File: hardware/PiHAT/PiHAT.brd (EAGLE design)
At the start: 65 x 56.5 mm, 41 parts, among them U1 ATMEGA328P, U2 TSL2561, U3 OPA344, U4 MPL115A, U6 ADMP401, U7 SHT31-DIS, Y1 16MHZ

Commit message: Update
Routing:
- net GND: vias 3 -> 4
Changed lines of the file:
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@@
 <via x="27.3812" y="10.795" extent="1-16" drill="0.6"/>
 <via x="39.243" y="6.3246" extent="1-16" drill="0.6"/>
-<wire x1="26.6256" y1="21.0058" x2="28.2256" y2="21.0058" width="0" layer="19" extent="1-1"/>
+<via x="26.162" y="30.5308" extent="1-16" drill="0.6"/>
 </signal>
 <signal name="GPIO18">

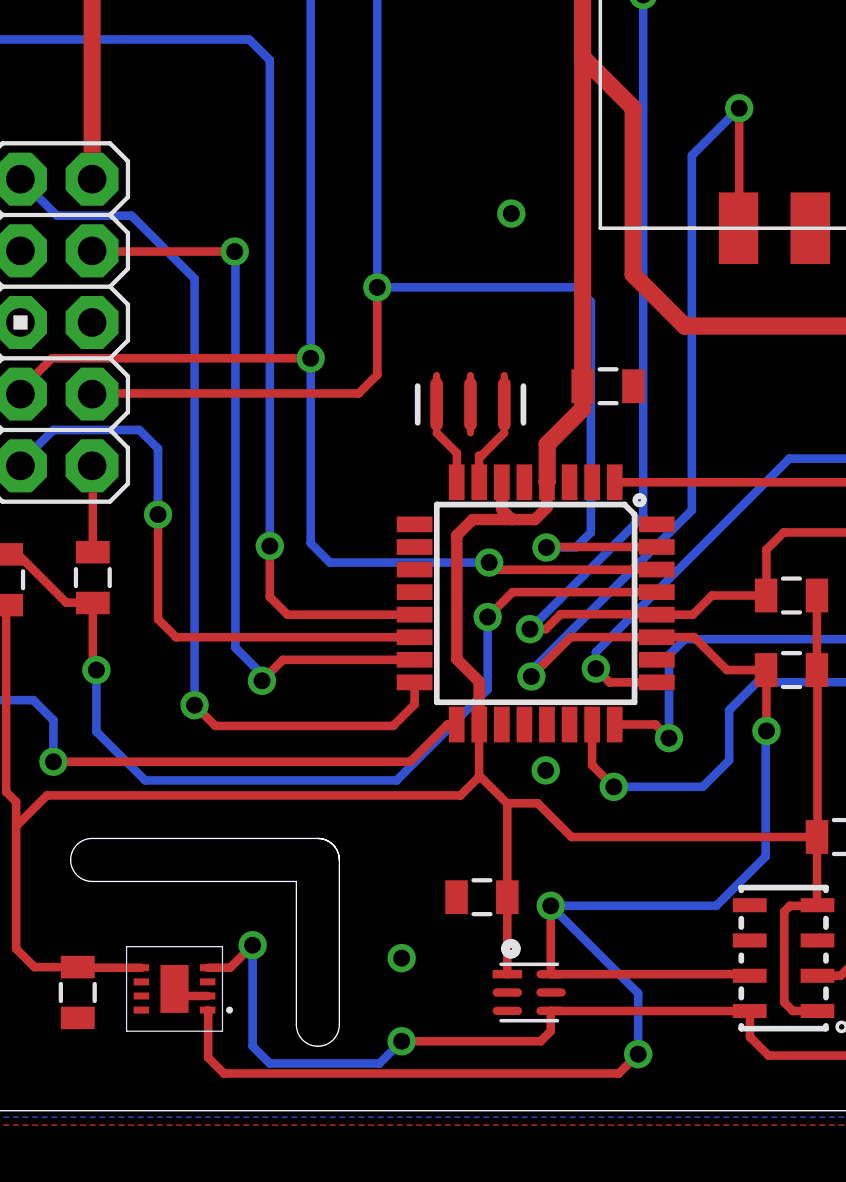
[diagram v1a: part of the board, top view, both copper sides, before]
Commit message: Moved Trace on PiAQ, v4 of enclosure
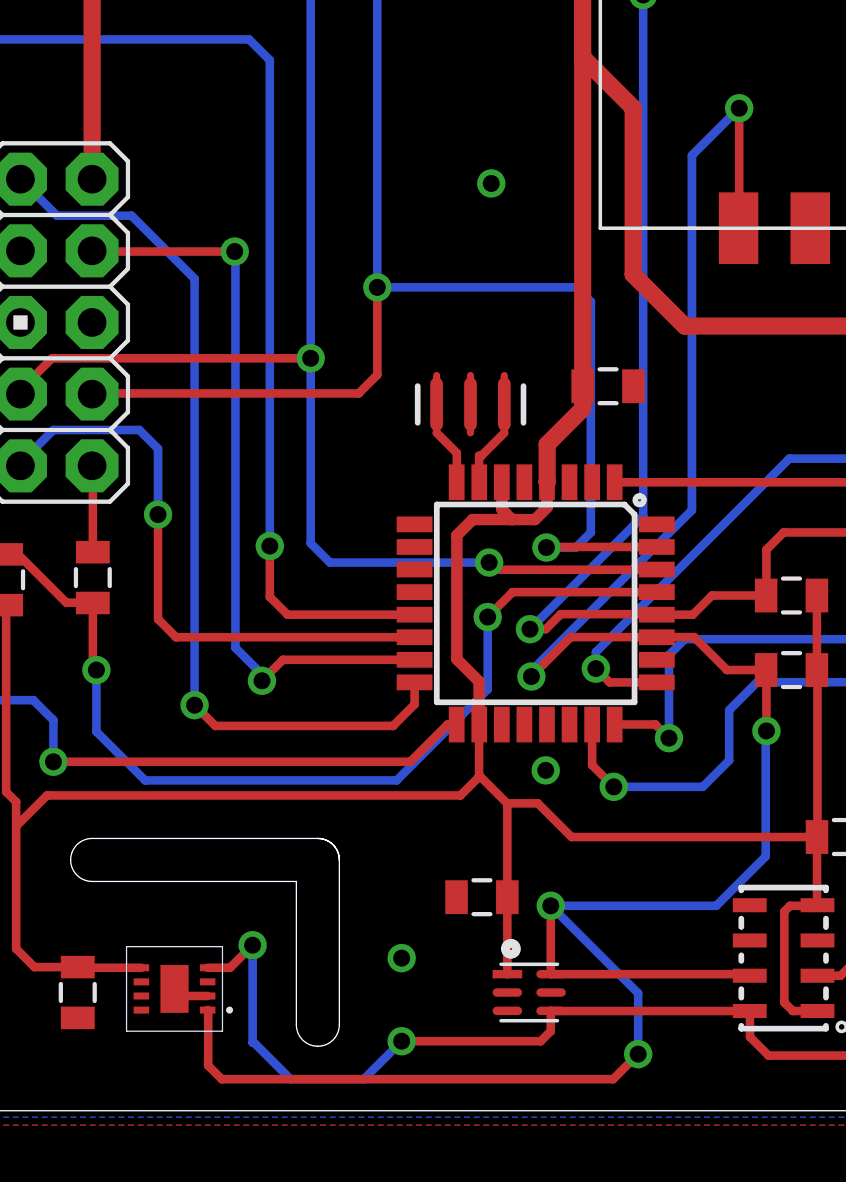
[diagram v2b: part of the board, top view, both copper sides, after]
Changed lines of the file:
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@@
 <layer number="23" name="tOrigins" color="14" fill="1" visible="yes" active="yes"/>
 <layer number="24" name="bOrigins" color="15" fill="1" visible="yes" active="yes"/>
-<layer number="25" name="tNames" color="7" fill="1" visible="yes" active="yes"/>
-<layer number="26" name="bNames" color="7" fill="1" visible="yes" active="yes"/>
-<layer number="27" name="tValues" color="7" fill="1" visible="yes" active="yes"/>
-<layer number="28" name="bValues" color="7" fill="1" visible="yes" active="yes"/>
+<layer number="25" name="tNames" color="7" fill="1" visible="no" active="yes"/>
+<layer number="26" name="bNames" color="7" fill="1" visible="no" active="yes"/>
+<layer number="27" name="tValues" color="7" fill="1" visible="no" active="yes"/>
+<layer number="28" name="bValues" color="7" fill="1" visible="no" active="yes"/>
 <layer number="29" name="tStop" color="7" fill="3" visible="no" active="yes"/>
 <layer number="30" name="bStop" color="7" fill="6" visible="no" active="yes"/>
@@
 <layer number="118" name="Rect_Pads" color="7" fill="1" visible="no" active="yes"/>
 <layer number="121" name="sName" color="7" fill="1" visible="yes" active="yes"/>
-<layer number="122" name="_bPlace" color="7" fill="1" visible="yes" active="yes"/>
+<layer number="122" name="_bPlace" color="7" fill="1" visible="no" active="yes"/>
 <layer number="123" name="tTestmark" color="7" fill="1" visible="no" active="yes"/>
 <layer number="124" name="bTestmark" color="7" fill="1" visible="no" active="yes"/>
@@
 <layer number="155" name="FabDoc3" color="7" fill="15" visible="no" active="no"/>
 <layer number="199" name="Contour" color="7" fill="1" visible="no" active="yes"/>
-<layer number="200" name="200bmp" color="1" fill="10" visible="yes" active="yes"/>
+<layer number="200" name="200bmp" color="1" fill="10" visible="no" active="yes"/>
 <layer number="201" name="201bmp" color="7" fill="1" visible="no" active="yes"/>
 <layer number="202" name="202bmp" color="7" fill="1" visible="no" active="yes"/>
@@
 <layer number="223" name="223bmp" color="24" fill="1" visible="no" active="no"/>
 <layer number="224" name="224bmp" color="25" fill="1" visible="no" active="no"/>
-<layer number="225" name="225bmp" color="7" fill="1" visible="yes" active="yes"/>
-<layer number="226" name="226bmp" color="7" fill="1" visible="yes" active="yes"/>
-<layer number="227" name="227bmp" color="7" fill="1" visible="yes" active="yes"/>
-<layer number="228" name="228bmp" color="7" fill="1" visible="yes" active="yes"/>
-<layer number="229" name="229bmp" color="7" fill="1" visible="yes" active="yes"/>
-<layer number="230" name="230bmp" color="7" fill="1" visible="yes" active="yes"/>
-<layer number="231" name="231bmp" color="7" fill="1" visible="yes" active="yes"/>
+<layer number="225" name="225bmp" color="7" fill="1" visible="no" active="yes"/>
+<layer number="226" name="226bmp" color="7" fill="1" visible="no" active="yes"/>
+<layer number="227" name="227bmp" color="7" fill="1" visible="no" active="yes"/>
+<layer number="228" name="228bmp" color="7" fill="1" visible="no" active="yes"/>
+<layer number="229" name="229bmp" color="7" fill="1" visible="no" active="yes"/>
+<layer number="230" name="230bmp" color="7" fill="1" visible="no" active="yes"/>
+<layer number="231" name="231bmp" color="7" fill="1" visible="no" active="yes"/>
 <layer number="232" name="Eagle3D_PG2" color="7" fill="1" visible="no" active="no"/>
 <layer number="233" name="Eagle3D_PG3" color="7" fill="1" visible="no" active="no"/>
@@
 <layer number="251" name="SMDround" color="7" fill="1" visible="no" active="yes"/>
 <layer number="254" name="cooling" color="7" fill="1" visible="no" active="yes"/>
-<layer number="255" name="routoute" color="7" fill="1" visible="yes" active="yes"/>
+<layer number="255" name="routoute" color="7" fill="1" visible="no" active="yes"/>
 </layers>
 <board>
@@
 <wire x1="27.559" y1="5.9944" x2="27.559" y2="3.584" width="0.3048" layer="1"/>
 <wire x1="27.559" y1="3.584" x2="27.572" y2="3.571" width="0.3048" layer="1"/>
-<wire x1="15.9766" y1="0.0508" x2="15.4178" y2="0.6096" width="0.3048" layer="1"/>
-<wire x1="15.4178" y1="0.6096" x2="15.4178" y2="2.2792" width="0.3048" layer="1"/>
+<wire x1="15.4178" y1="0.3302" x2="15.4178" y2="2.2792" width="0.3048" layer="1"/>
 <wire x1="15.4178" y1="2.2792" x2="15.399" y2="2.298" width="0.3048" layer="1"/>
 <wire x1="35.1934" y1="14.351" x2="33.8074" y2="14.351" width="0.3048" layer="1"/>
@@
 <wire x1="34.2392" y1="34.2646" x2="34.2392" y2="30.0342" width="0.3048" layer="1"/>
 <wire x1="34.2392" y1="30.0342" x2="34.217" y2="30.012" width="0.3048" layer="1"/>
-<wire x1="15.9766" y1="0.0508" x2="29.972" y2="0.0508" width="0.3048" layer="1"/>
-<wire x1="29.972" y1="0.0508" x2="30.6578" y2="0.7366" width="0.3048" layer="1"/>
 <via x="30.6578" y="0.7366" extent="1-16" drill="0.6"/>
 <wire x1="30.6578" y1="0.7366" x2="30.6578" y2="2.8956" width="0.3048" layer="16"/>
 <wire x1="30.6578" y1="2.8956" x2="27.559" y2="5.9944" width="0.3048" layer="16"/>
+<wire x1="30.6578" y1="0.7366" x2="29.7688" y2="-0.1524" width="0.3048" layer="1"/>
+<wire x1="15.4178" y1="0.3302" x2="15.9004" y2="-0.1524" width="0.3048" layer="1"/>
+<wire x1="15.9004" y1="-0.1524" x2="29.7688" y2="-0.1524" width="0.3048" layer="1"/>
 </signal>
 <signal name="SCL">
@@
 <wire x1="16.1932" y1="3.798" x2="16.9926" y2="4.5974" width="0.3048" layer="1"/>
 <via x="16.9926" y="4.5974" extent="1-16" drill="0.6"/>
-<wire x1="16.9926" y1="4.5974" x2="16.9926" y2="1.016" width="0.3048" layer="16"/>
-<wire x1="16.9926" y1="1.016" x2="17.6022" y2="0.4064" width="0.3048" layer="16"/>
-<wire x1="17.6022" y1="0.4064" x2="21.4884" y2="0.4064" width="0.3048" layer="16"/>
-<wire x1="21.4884" y1="0.4064" x2="22.2758" y2="1.1938" width="0.3048" layer="16"/>
 <via x="22.2758" y="1.1938" extent="1-16" drill="0.6"/>
 <wire x1="22.2758" y1="1.1938" x2="27.2034" y2="1.1938" width="0.3048" layer="1"/>
@@
 <wire x1="35.7886" y1="38.3032" x2="30.861" y2="38.3032" width="0.3048" layer="1"/>
 <wire x1="30.861" y1="38.3032" x2="30.8356" y2="38.2778" width="0.3048" layer="1"/>
+<wire x1="16.9926" y1="4.5974" x2="16.9926" y2="1.143" width="0.3048" layer="16"/>
+<wire x1="16.9926" y1="1.143" x2="17.0434" y2="1.143" width="0.3048" layer="16"/>
+<wire x1="17.0434" y1="1.143" x2="18.3388" y2="-0.1524" width="0.3048" layer="16"/>
+<wire x1="18.3388" y1="-0.1524" x2="20.9296" y2="-0.1524" width="0.3048" layer="16"/>
+<wire x1="20.9296" y1="-0.1524" x2="22.2758" y2="1.1938" width="0.3048" layer="16"/>
 </signal>
 <signal name="GPIO4">
@@
 <via x="27.3812" y="10.795" extent="1-16" drill="0.6"/>
 <via x="39.243" y="6.3246" extent="1-16" drill="0.6"/>
-<via x="26.162" y="30.5308" extent="1-16" drill="0.6"/>
+<via x="25.4508" y="31.5976" extent="1-16" drill="0.6"/>
 </signal>
 <signal name="GPIO18">
